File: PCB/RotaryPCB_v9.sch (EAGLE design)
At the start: 4 parts

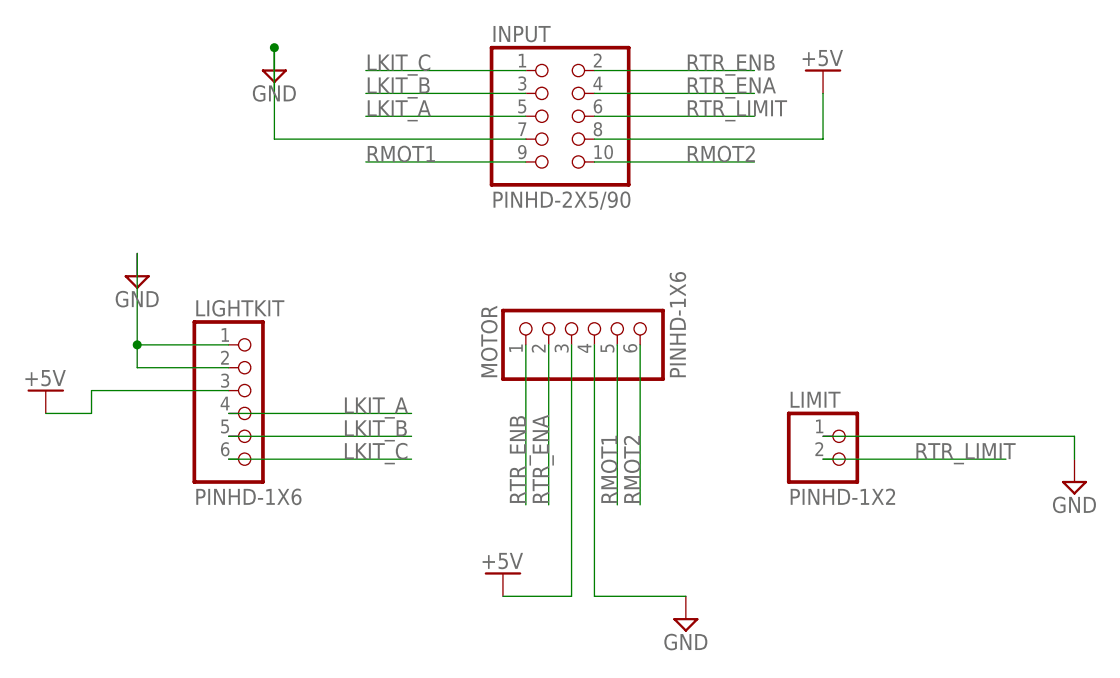
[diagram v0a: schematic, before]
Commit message: This version uses thicker traces and adds a copper pour. The lifter board is a four layer board. The order of the connection pins on the rotary has changed. Do NOT use the same cable as the older board. The order was changed to allow using a silicone ribbon cable.
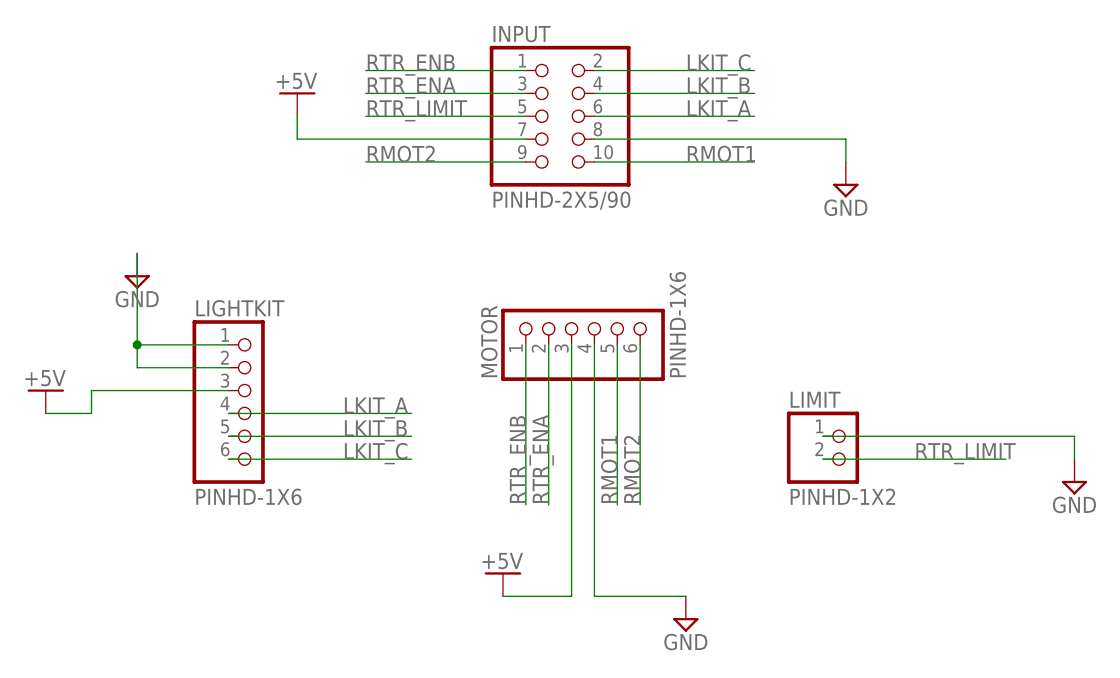
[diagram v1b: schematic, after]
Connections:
- net +5V: now also INPUT.7; no longer INPUT.8
- net GND: now also INPUT.8; no longer INPUT.7
- net LKIT_A: now also INPUT.6; no longer INPUT.5
- net LKIT_B: now also INPUT.4; no longer INPUT.3
- net LKIT_C: now also INPUT.2; no longer INPUT.1
- net RMOT1: now also INPUT.10; no longer INPUT.9
- net RMOT2: now also INPUT.9; no longer INPUT.10
- net RTR_ENA: now also INPUT.3; no longer INPUT.4
- net RTR_ENB: now also INPUT.1; no longer INPUT.2
- net RTR_LIMIT: now also INPUT.5; no longer INPUT.6
